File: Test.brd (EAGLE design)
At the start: 43.2 x 53 mm, 12 parts

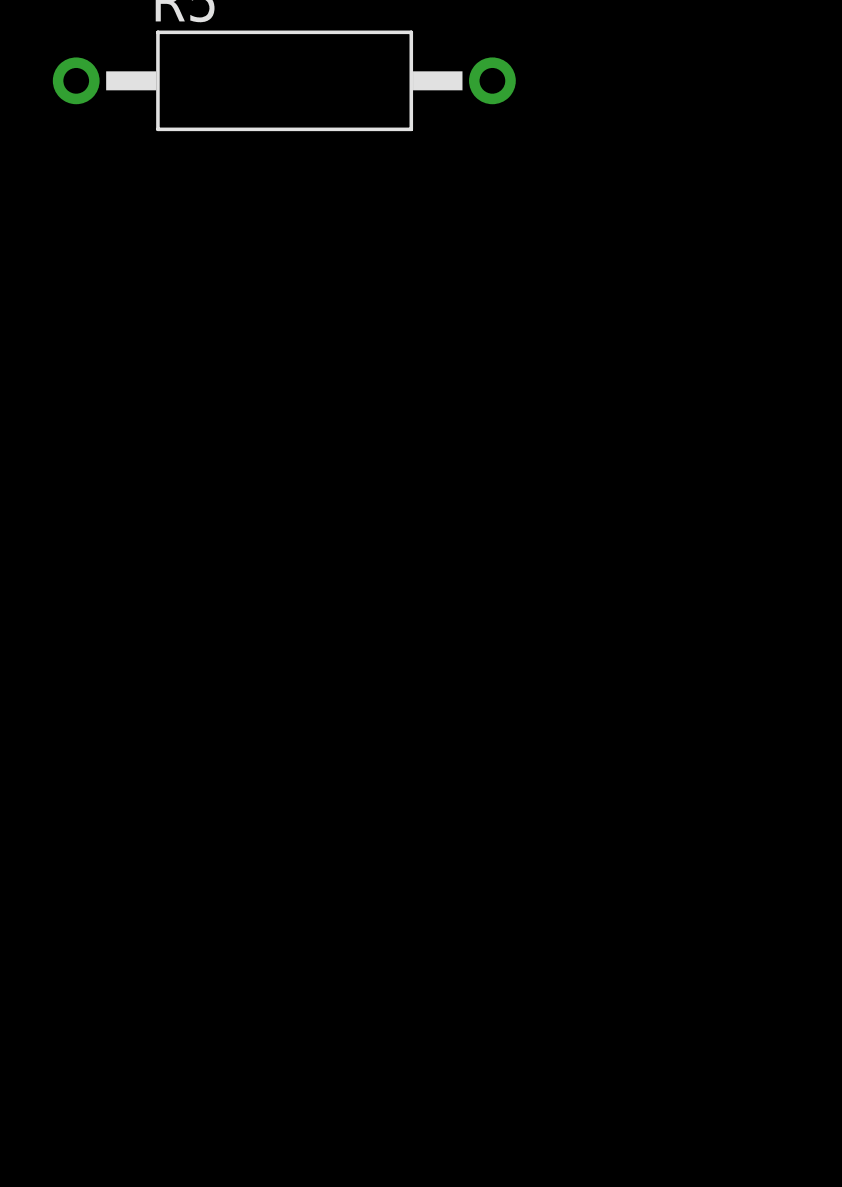
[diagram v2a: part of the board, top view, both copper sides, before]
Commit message: [add]LM3914にこめ
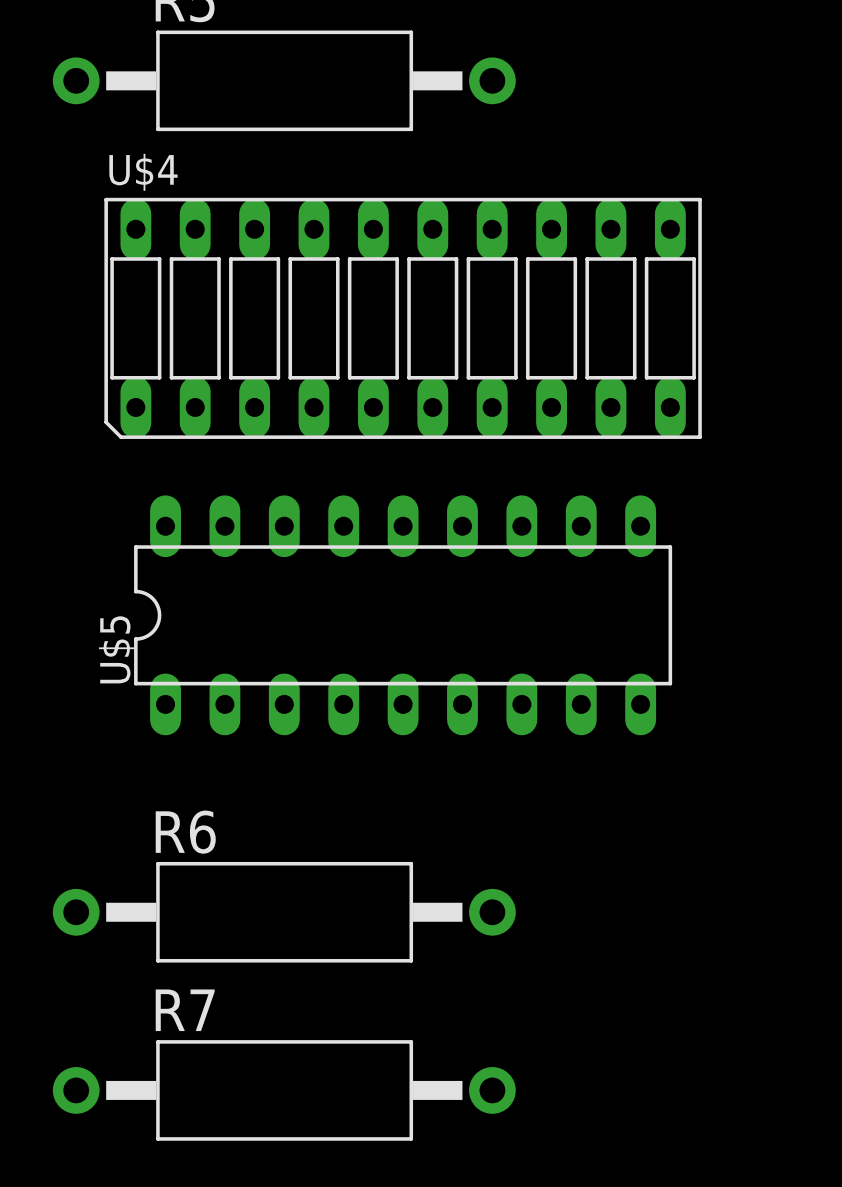
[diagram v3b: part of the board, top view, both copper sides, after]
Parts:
- added R6, R7: (no value), resistor-power:AC01
- added U$4: LB10, SpectralAnalyzer:LB10
- added U$5: LM3914, SpectralAnalyzer:DIL18
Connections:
- new net N$20: U$4.11, U$5.1
- new net N$23: U$4.12, U$5.10
- new net N$24: U$4.13, U$5.11
- new net N$25: U$4.14, U$5.12
- new net N$26: U$4.15, U$5.13
- new net N$27: U$4.16, U$5.14
- new net N$28: U$4.17, U$5.15
- new net N$29: U$4.18, U$5.16
- new net N$30: U$4.19, U$5.17
- new net N$31: U$4.20, U$5.18
- new net N$32: U$5.5
- new net N$33: R6.2, U$5.6, U$5.7
- new net N$34: R6.1, R7.2, U$5.8
- net +12V: now also U$5.3, U$5.9
- net +5V: now also U$4.1, U$4.10, U$4.2, U$4.3, U$4.4, U$4.5, U$4.6, U$4.7, U$4.8, U$4.9
- net GND: now also R7.1, U$5.2, U$5.4
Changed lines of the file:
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@@
 <attribute name="VALUE" x="5.715" y="-56.515" size="1.778" layer="27" ratio="10"/>
+</element>
+<element name="U$4" library="SpectralAnalyzer" library_urn="urn:adsk.eagle:library:7692814" package="LB10" package3d_urn="urn:adsk.eagle:package:7691019/2" value="LB10" x="15.24" y="-66.04" smashed="yes">
+<attribute name="NAME" x="2.54" y="-60.325" size="1.27" layer="25" ratio="10"/>
+<attribute name="VALUE" x="11.43" y="-60.325" size="1.27" layer="27" ratio="10"/>
+</element>
+<element name="U$5" library="SpectralAnalyzer" library_urn="urn:adsk.eagle:library:7692814" package="DIL18" package3d_urn="urn:adsk.eagle:package:7691020/2" value="LM3914" x="15.24" y="-78.74" smashed="yes">
+<attribute name="NAME" x="3.556" y="-81.788" size="1.27" layer="25" ratio="10" rot="R90"/>
+<attribute name="VALUE" x="5.715" y="-79.375" size="1.27" layer="27" ratio="10"/>
+</element>
+<element name="R6" library="resistor-power" library_urn="urn:adsk.eagle:library:344" package="AC01" package3d_urn="urn:adsk.eagle:package:25124/1" value="" x="10.16" y="-91.44" smashed="yes">
+<attribute name="MF" value="" x="10.16" y="-91.44" size="1.778" layer="27" display="off"/>
+<attribute name="MPN" value="" x="10.16" y="-91.44" size="1.778" layer="27" display="off"/>
+<attribute name="NAME" x="4.445" y="-88.9" size="1.778" layer="25" ratio="10"/>
+<attribute name="OC_FARNELL" value="unknown" x="10.16" y="-91.44" size="1.778" layer="27" display="off"/>
+<attribute name="OC_NEWARK" value="unknown" x="10.16" y="-91.44" size="1.778" layer="27" display="off"/>
+<attribute name="VALUE" x="5.715" y="-92.075" size="1.778" layer="27" ratio="10"/>
+</element>
+<element name="R7" library="resistor-power" library_urn="urn:adsk.eagle:library:344" package="AC01" package3d_urn="urn:adsk.eagle:package:25124/1" value="" x="10.16" y="-99.06" smashed="yes">
+<attribute name="MF" value="" x="10.16" y="-99.06" size="1.778" layer="27" display="off"/>
+<attribute name="MPN" value="" x="10.16" y="-99.06" size="1.778" layer="27" display="off"/>
+<attribute name="NAME" x="4.445" y="-96.52" size="1.778" layer="25" ratio="10"/>
+<attribute name="OC_FARNELL" value="unknown" x="10.16" y="-99.06" size="1.778" layer="27" display="off"/>
+<attribute name="OC_NEWARK" value="unknown" x="10.16" y="-99.06" size="1.778" layer="27" display="off"/>
+<attribute name="VALUE" x="5.715" y="-99.695" size="1.778" layer="27" ratio="10"/>
 </element>
 </elements>
@@
 <contactref element="U$2" pad="6"/>
 <contactref element="U$2" pad="7"/>
-<wire x1="15.6845" y1="39.624" x2="34.671" y2="38.7985" width="0" layer="19" extent="16-16"/>
-<wire x1="3.81" y1="-11.43" x2="15.6845" y2="39.624" width="0" layer="19" extent="16-16"/>
-<wire x1="3.81" y1="-26.67" x2="3.81" y2="-11.43" width="0" layer="19" extent="1-1"/>
+<contactref element="U$4" pad="5"/>
+<contactref element="U$4" pad="1"/>
+<contactref element="U$4" pad="2"/>
+<contactref element="U$4" pad="3"/>
+<contactref element="U$4" pad="4"/>
+<contactref element="U$4" pad="8"/>
+<contactref element="U$4" pad="9"/>
+<contactref element="U$4" pad="10"/>
+<contactref element="U$4" pad="6"/>
+<contactref element="U$4" pad="7"/>
+<wire x1="6.35" y1="-69.85" x2="3.81" y2="-69.85" width="0" layer="19" extent="1-1"/>
+<wire x1="8.89" y1="-69.85" x2="6.35" y2="-69.85" width="0" layer="19" extent="1-1"/>
+<wire x1="11.43" y1="-69.85" x2="8.89" y2="-69.85" width="0" layer="19" extent="1-1"/>
+<wire x1="13.97" y1="-69.85" x2="11.43" y2="-69.85" width="0" layer="19" extent="1-1"/>
+<wire x1="16.51" y1="-69.85" x2="13.97" y2="-69.85" width="0" layer="19" extent="1-1"/>
+<wire x1="19.05" y1="-69.85" x2="16.51" y2="-69.85" width="0" layer="19" extent="1-1"/>
+<wire x1="21.59" y1="-69.85" x2="19.05" y2="-69.85" width="0" layer="19" extent="1-1"/>
+<wire x1="24.13" y1="-69.85" x2="21.59" y2="-69.85" width="0" layer="19" extent="1-1"/>
+<wire x1="26.67" y1="-69.85" x2="24.13" y2="-69.85" width="0" layer="19" extent="1-1"/>
+<wire x1="3.81" y1="-26.67" x2="3.81" y2="-69.85" width="0" layer="19" extent="1-1"/>
 <wire x1="6.35" y1="-26.67" x2="3.81" y2="-26.67" width="0" layer="19" extent="1-1"/>
 <wire x1="8.89" y1="-26.67" x2="6.35" y2="-26.67" width="0" layer="19" extent="1-1"/>
@@
 <wire x1="24.13" y1="-26.67" x2="21.59" y2="-26.67" width="0" layer="19" extent="1-1"/>
 <wire x1="26.67" y1="-26.67" x2="24.13" y2="-26.67" width="0" layer="19" extent="1-1"/>
+<wire x1="3.81" y1="-11.43" x2="3.81" y2="-26.67" width="0" layer="19" extent="1-1"/>
+<wire x1="15.6845" y1="39.624" x2="3.81" y2="-11.43" width="0" layer="19" extent="16-16"/>
+<wire x1="34.671" y1="38.7985" x2="15.6845" y2="39.624" width="0" layer="19" extent="16-16"/>
 </signal>
 <signal name="GND">
@@
 <contactref element="U$3" pad="4"/>
 <contactref element="R5" pad="1"/>
+<contactref element="U$5" pad="2"/>
+<contactref element="U$5" pad="4"/>
+<contactref element="R7" pad="1"/>
+<wire x1="7.62" y1="-82.55" x2="1.26" y2="-99.06" width="0" layer="19" extent="1-1"/>
+<wire x1="12.7" y1="-82.55" x2="7.62" y2="-82.55" width="0" layer="19" extent="1-1"/>
+<wire x1="1.26" y1="-55.88" x2="7.62" y2="-82.55" width="0" layer="19" extent="1-1"/>
 <wire x1="7.62" y1="-39.37" x2="1.26" y2="-55.88" width="0" layer="19" extent="1-1"/>
 <wire x1="12.7" y1="-39.37" x2="7.62" y2="-39.37" width="0" layer="19" extent="1-1"/>
@@
 <contactref element="U$3" pad="3"/>
 <contactref element="U$3" pad="9"/>
+<contactref element="U$5" pad="3"/>
+<contactref element="U$5" pad="9"/>
+<wire x1="25.4" y1="-82.55" x2="10.16" y2="-82.55" width="0" layer="19" extent="1-1"/>
+<wire x1="10.16" y1="-39.37" x2="10.16" y2="-82.55" width="0" layer="19" extent="1-1"/>
 <wire x1="25.4" y1="-39.37" x2="10.16" y2="-39.37" width="0" layer="19" extent="1-1"/>
 </signal>
@@
 <wire x1="22.86" y1="-39.37" x2="19.06" y2="-55.88" width="0" layer="19" extent="1-1"/>
 </signal>
+<signal name="N$20">
+<contactref element="U$4" pad="11"/>
+<contactref element="U$5" pad="1"/>
+<wire x1="26.67" y1="-62.23" x2="5.08" y2="-82.55" width="0" layer="19" extent="1-1"/>
+</signal>
+<signal name="N$23">
+<contactref element="U$4" pad="12"/>
+<contactref element="U$5" pad="10"/>
+<wire x1="24.13" y1="-62.23" x2="25.4" y2="-74.93" width="0" layer="19" extent="1-1"/>
+</signal>
+<signal name="N$24">
+<contactref element="U$4" pad="13"/>
+<contactref element="U$5" pad="11"/>
+<wire x1="21.59" y1="-62.23" x2="22.86" y2="-74.93" width="0" layer="19" extent="1-1"/>
+</signal>
+<signal name="N$25">
+<contactref element="U$4" pad="14"/>
+<contactref element="U$5" pad="12"/>
+<wire x1="19.05" y1="-62.23" x2="20.32" y2="-74.93" width="0" layer="19" extent="1-1"/>
+</signal>
+<signal name="N$26">
+<contactref element="U$4" pad="15"/>
+<contactref element="U$5" pad="13"/>
+<wire x1="16.51" y1="-62.23" x2="17.78" y2="-74.93" width="0" layer="19" extent="1-1"/>
+</signal>
+<signal name="N$27">
+<contactref element="U$4" pad="16"/>
+<contactref element="U$5" pad="14"/>
+<wire x1="13.97" y1="-62.23" x2="15.24" y2="-74.93" width="0" layer="19" extent="1-1"/>
+</signal>
+<signal name="N$28">
+<contactref element="U$4" pad="17"/>
+<contactref element="U$5" pad="15"/>
+<wire x1="11.43" y1="-62.23" x2="12.7" y2="-74.93" width="0" layer="19" extent="1-1"/>
+</signal>
+<signal name="N$29">
+<contactref element="U$4" pad="18"/>
+<contactref element="U$5" pad="16"/>
+<wire x1="8.89" y1="-62.23" x2="10.16" y2="-74.93" width="0" layer="19" extent="1-1"/>
+</signal>
+<signal name="N$30">
+<contactref element="U$4" pad="19"/>
+<contactref element="U$5" pad="17"/>
+<wire x1="6.35" y1="-62.23" x2="7.62" y2="-74.93" width="0" layer="19" extent="1-1"/>
+</signal>
+<signal name="N$31">
+<contactref element="U$4" pad="20"/>
+<contactref element="U$5" pad="18"/>
+<wire x1="3.81" y1="-62.23" x2="5.08" y2="-74.93" width="0" layer="19" extent="1-1"/>
+</signal>
+<signal name="N$32">
+<contactref element="U$5" pad="5"/>
+</signal>
+<signal name="N$33">
+<contactref element="U$5" pad="7"/>
+<contactref element="U$5" pad="6"/>
+<contactref element="R6" pad="2"/>
+<wire x1="17.78" y1="-82.55" x2="19.06" y2="-91.44" width="0" layer="19" extent="1-1"/>
+<wire x1="20.32" y1="-82.55" x2="17.78" y2="-82.55" width="0" layer="19" extent="1-1"/>
+</signal>
+<signal name="N$34">
+<contactref element="R6" pad="1"/>
+<contactref element="R7" pad="2"/>
+<contactref element="U$5" pad="8"/>
+<wire x1="19.06" y1="-99.06" x2="1.26" y2="-91.44" width="0" layer="19" extent="1-1"/>
+<wire x1="22.86" y1="-82.55" x2="19.06" y2="-99.06" width="0" layer="19" extent="1-1"/>
+</signal>
 </signals>

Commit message: [add]esp32
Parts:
- added U1: ESP-WROOM-32, SpectralAnalyzer:ESP-WROOM-32
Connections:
- new net N$35: U1.5
- new net N$36: U1.6
- new net N$37: U1.7
- new net N$38: U1.14
- new net N$39: U1.15
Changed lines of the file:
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@@
 <attribute name="VALUE" x="5.715" y="-99.695" size="1.778" layer="27" ratio="10"/>
+</element>
+<element name="U1" library="SpectralAnalyzer" library_urn="urn:adsk.eagle:library:7692814" package="ESP-WROOM-32" package3d_urn="urn:adsk.eagle:package:8041332/1" value="ESP-WROOM-32" x="12.7" y="-111.76" smashed="yes">
+<attribute name="NAME" x="4.94" y="-111.76" size="0.8128" layer="25" rot="R90" align="center"/>
+<attribute name="VALUE" x="6.21" y="-111.76" size="0.8128" layer="27" rot="R90" align="center"/>
 </element>
 </elements>
@@
 <wire x1="22.86" y1="-82.55" x2="19.06" y2="-99.06" width="0" layer="19" extent="1-1"/>
 </signal>
+<signal name="N$35">
+<contactref element="U1" pad="5"/>
+</signal>
+<signal name="N$36">
+<contactref element="U1" pad="6"/>
+</signal>
+<signal name="N$37">
+<contactref element="U1" pad="7"/>
+</signal>
+<signal name="N$38">
+<contactref element="U1" pad="14"/>
+</signal>
+<signal name="N$39">
+<contactref element="U1" pad="15"/>
+</signal>
 </signals>

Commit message: [fix]手直し
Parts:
- moved R6 165.3 mm to (124.5, 27.9)
- moved U1 160.3 mm to (116.8, 10.2)
- moved R7 158.0 mm to (104.1, 27.9)
- moved U$4 150.8 mm to (96.5, 61.0)
- moved U$5 148.6 mm to (96.5, 45.7)
- moved R4 104.2 mm to (86.4, 22.9)
- moved U$2 100.7 mm to (71.1, 61.0)
- moved U$3 98.6 mm to (71.1, 45.7)
- moved R5 96.6 mm to (66.0, 22.9)
- moved U$1 41.0 mm to (43.2, 12.7)
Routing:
- removed copper zone on layer 16, net N$6
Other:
- board size 43.2 x 53 mm -> 139.7 x 73.3 mm
